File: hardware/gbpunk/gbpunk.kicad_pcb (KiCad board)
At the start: 2 copper layers, 51.4 x 61 mm, 50 parts, among them J1 CART, J4 SWD_CONNECTOR, P1 USB_C_CONNECTOR, SW7 RESET, SW9 USB_BOOT, U1 RP2040, U2 SN74LVC4245A, U3 W25Q128JVS, U4 NCP1117-3.3_SOT223, U5 SN74LVC4245A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

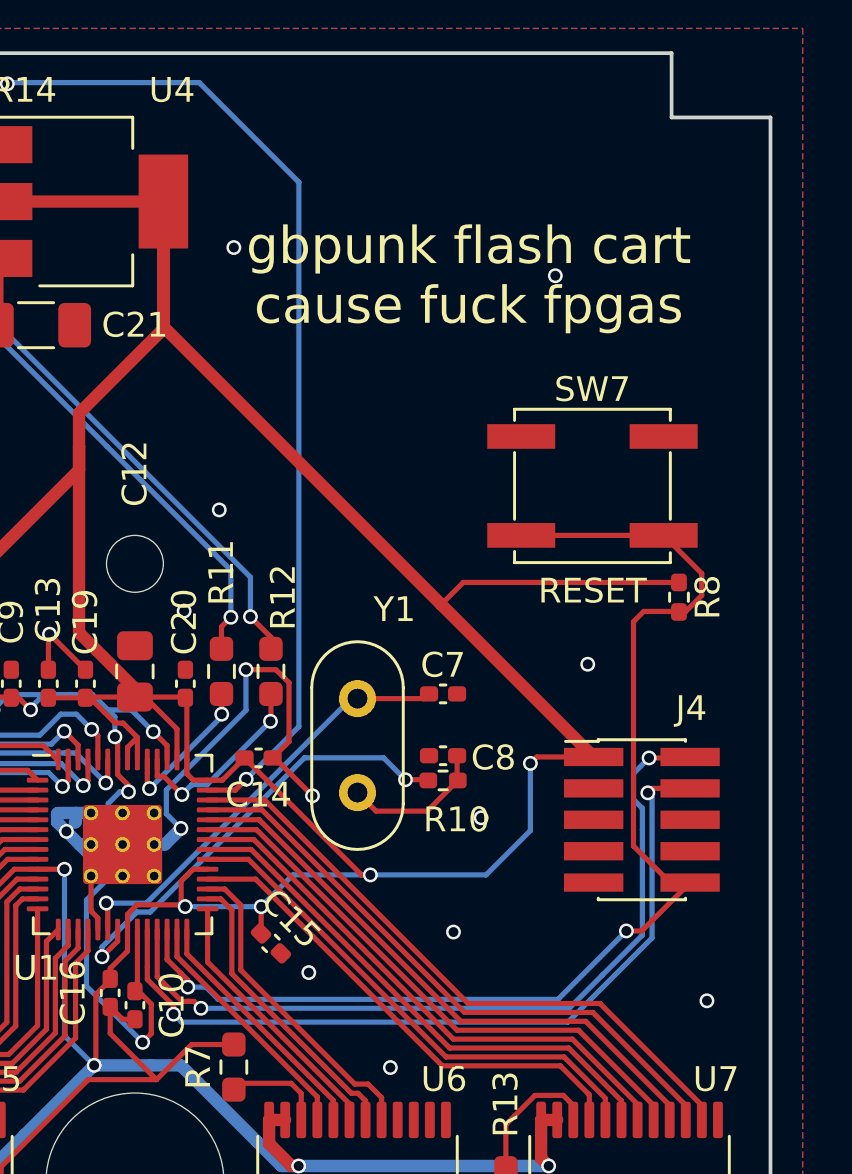
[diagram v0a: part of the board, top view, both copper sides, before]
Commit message: need an interposer to measure timings
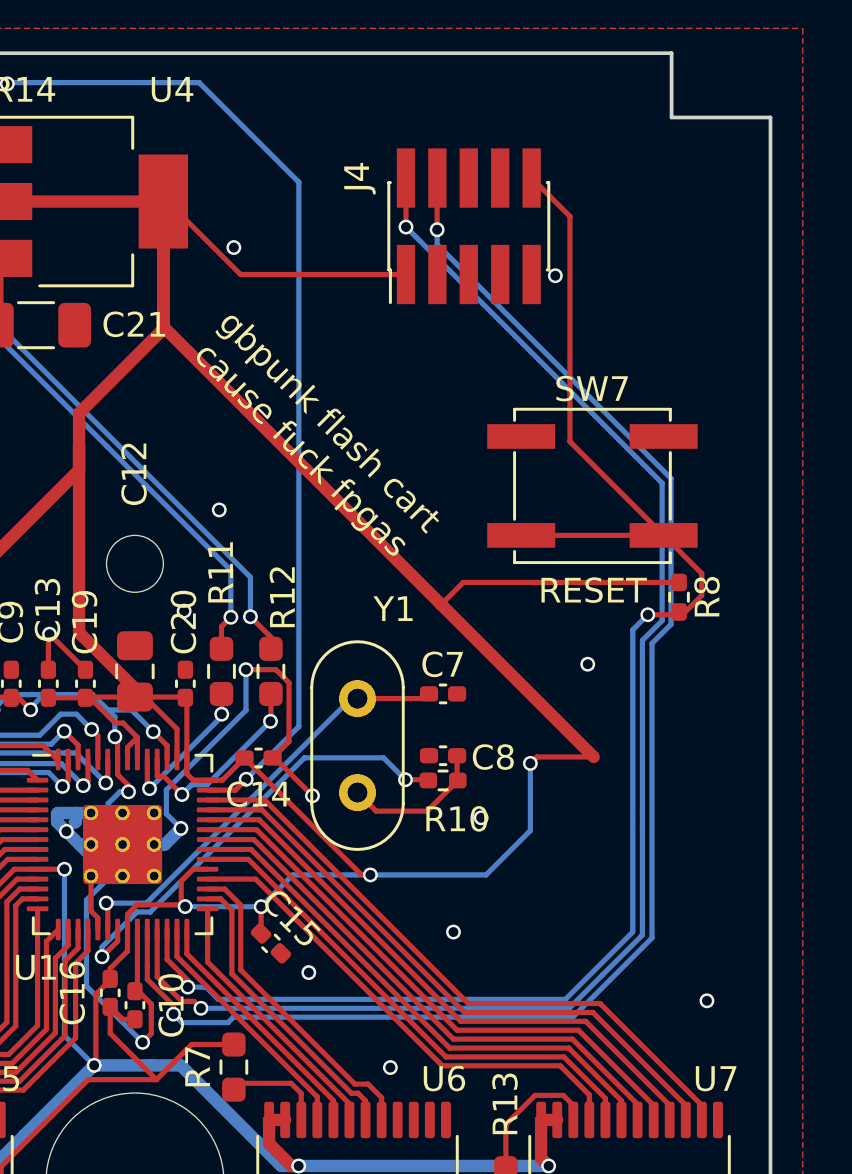
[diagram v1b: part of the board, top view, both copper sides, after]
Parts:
- moved J4 25.0 mm to (113.5, 46.0), turned to 90 degrees
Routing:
- net /SWCLK: track 32.5 -> 59.7 mm
- net /SWDIO: track 32.7 -> 58.7 mm
- net /RUN: track 49.2 -> 63.1 mm
- net +3.3V: track 293.3 -> 304.4 mm
